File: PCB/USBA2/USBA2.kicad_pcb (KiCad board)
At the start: 2 copper layers, 15.9 x 13.9 mm, 19 parts, among them J1 USB_A, J2 Shelly, U1 ESP32-PICO-MINI-02, U2 LMR16006YDDCR, U4 QR

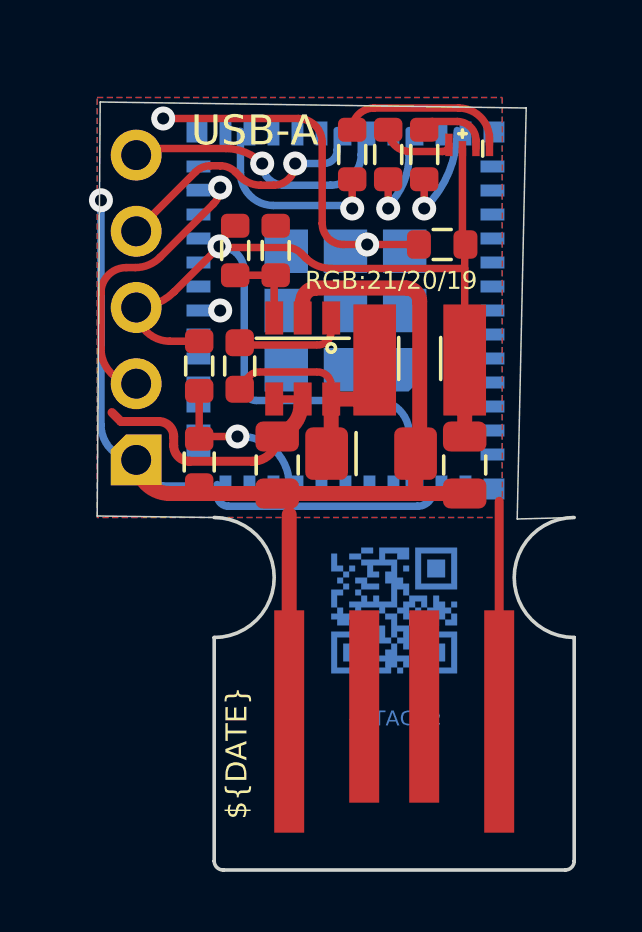
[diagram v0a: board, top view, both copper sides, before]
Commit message: Right angle version
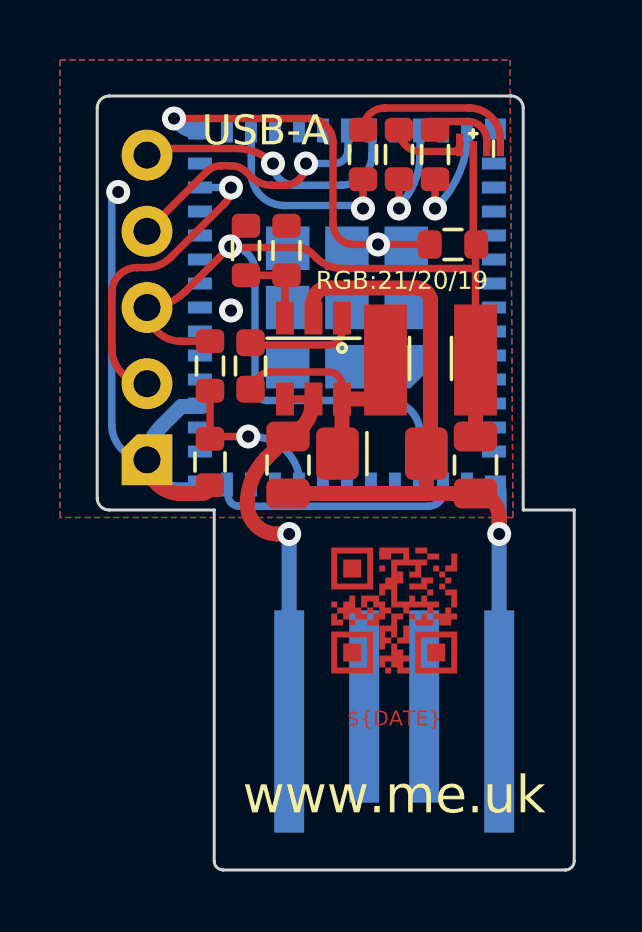
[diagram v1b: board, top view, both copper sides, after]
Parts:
- J1: moved to B.Cu
- U4: moved to F.Cu
- moved C1 0.36 mm to (116.7, 114.2)
- moved C2 0.36 mm to (118.0, 117.5)
- moved C3 0.36 mm to (124.2, 117.5)
- moved C4 0.36 mm to (123.5, 110.2)
- moved C5 0.36 mm to (115.4, 117.4)
- moved D1 0.36 mm to (124.4, 107.0)
- moved D2 0.36 mm to (121.1, 117.1)
- moved J2 0.36 mm to (113.3, 112.2)
- moved L1 0.36 mm to (122.7, 114.0)
- moved R1 0.36 mm to (122.9, 107.2)
- moved R2 0.36 mm to (120.5, 107.2)
- moved R3 0.36 mm to (121.7, 107.2)
- moved R4 0.36 mm to (116.6, 110.3)
- moved R5 0.36 mm to (117.9, 110.3)
- moved R6 0.36 mm to (115.4, 114.2)
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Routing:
- net GND: track 43.8 -> 47.4 mm, vias 4 -> 5
- net DC: track 15.2 -> 11.8 mm, vias 0 -> 1
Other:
- board size 15.9 x 13.9 mm -> 15.9 x 13.8 mm

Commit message: New layoput
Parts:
- moved D1 0.35 mm to (124.4, 107.3)
- moved R1 0.35 mm to (122.9, 107.5)
- moved R2 0.35 mm to (120.5, 107.5)
- moved R3 0.35 mm to (121.7, 107.5)
- moved J2 0.15 mm to (113.4, 112.2)
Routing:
- net GND: track 47.4 -> 71.6 mm, vias 5 -> 4
- net GPIO0: track 10.3 -> 9.70 mm
- net +3.3V: track 35.5 -> 34.9 mm
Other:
- board size 15.9 x 13.8 mm -> 15.4 x 13.4 mm
